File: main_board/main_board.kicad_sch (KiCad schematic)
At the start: 10 parts

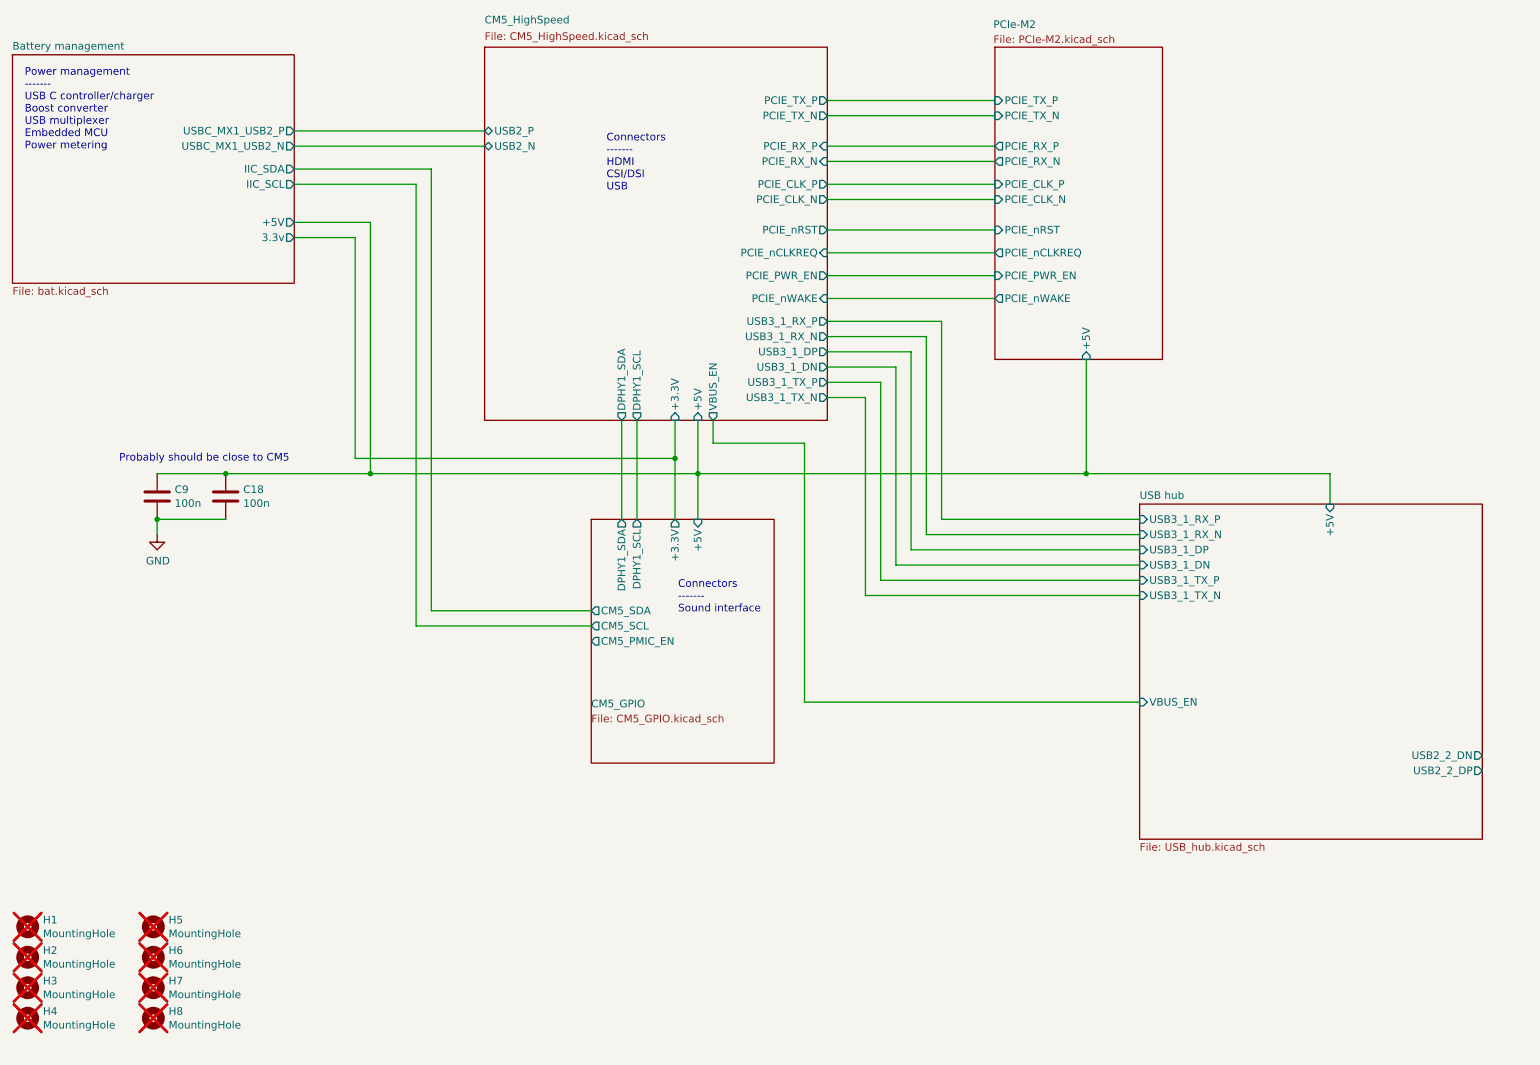
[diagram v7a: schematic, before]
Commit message: Add expansion slot
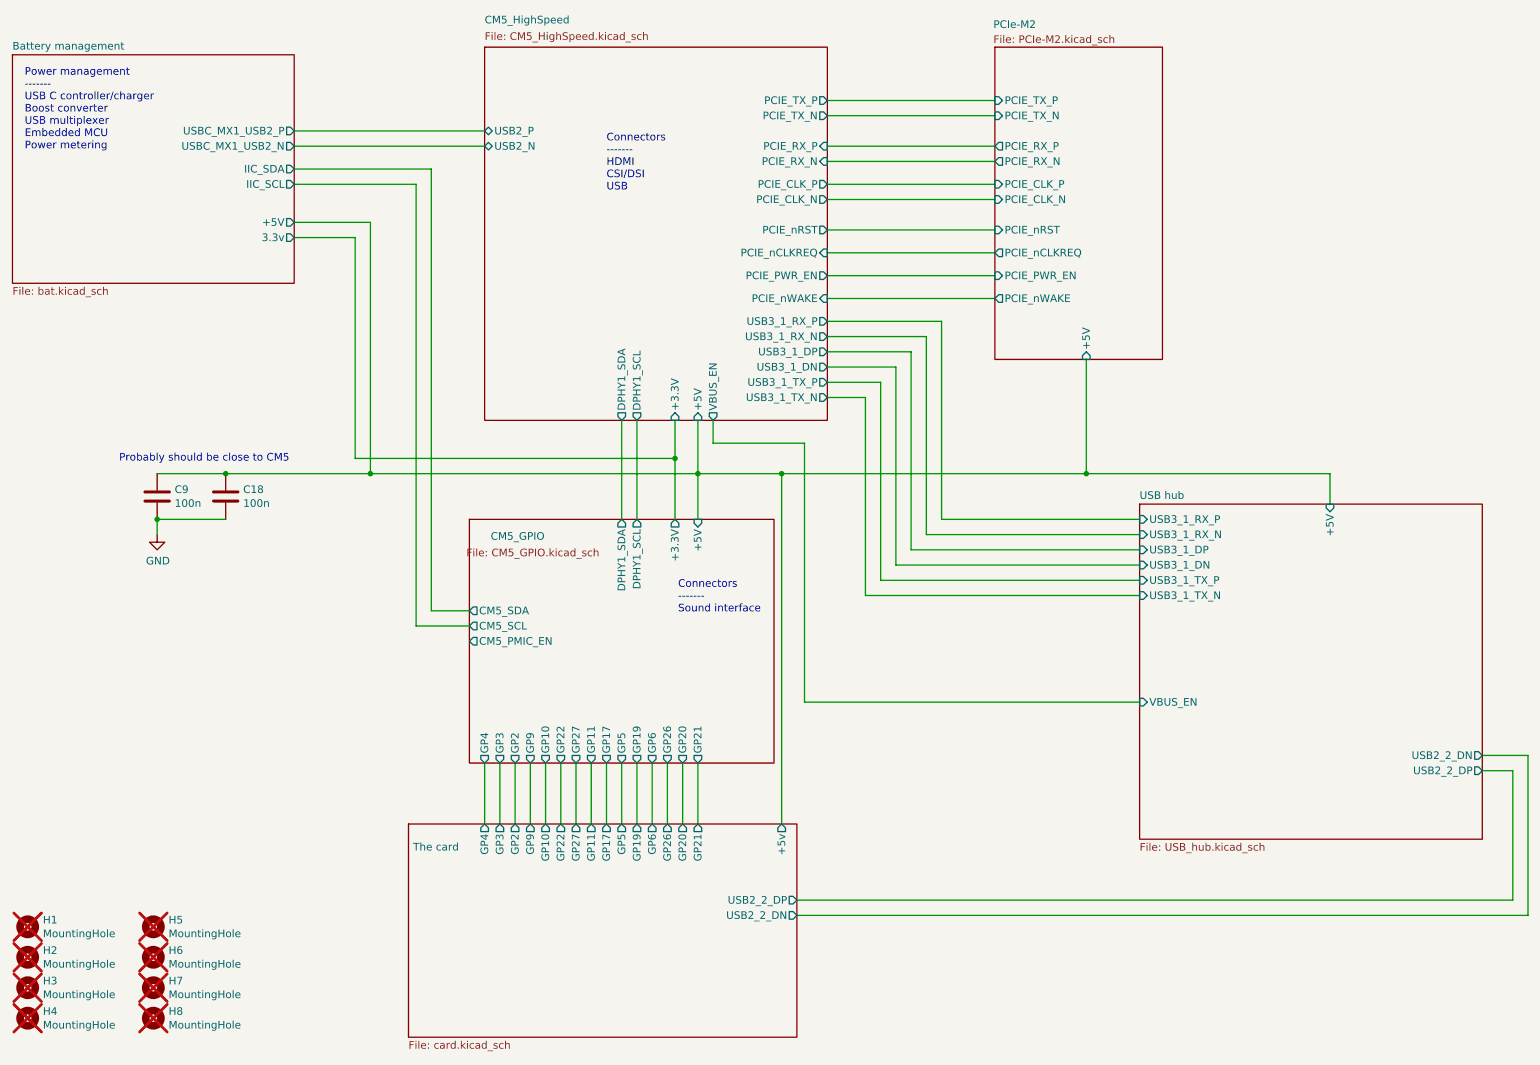
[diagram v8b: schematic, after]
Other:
- added sheet The card (card.kicad_sch)
- sheet CM5_GPIO ports: added GP10, GP11, GP17, GP19, GP2, GP20, GP21, GP22, GP26, GP27, GP3, GP4, GP5, GP6, GP9; removed none
